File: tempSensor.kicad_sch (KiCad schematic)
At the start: 5 parts, among them U2 TMP175AIDR

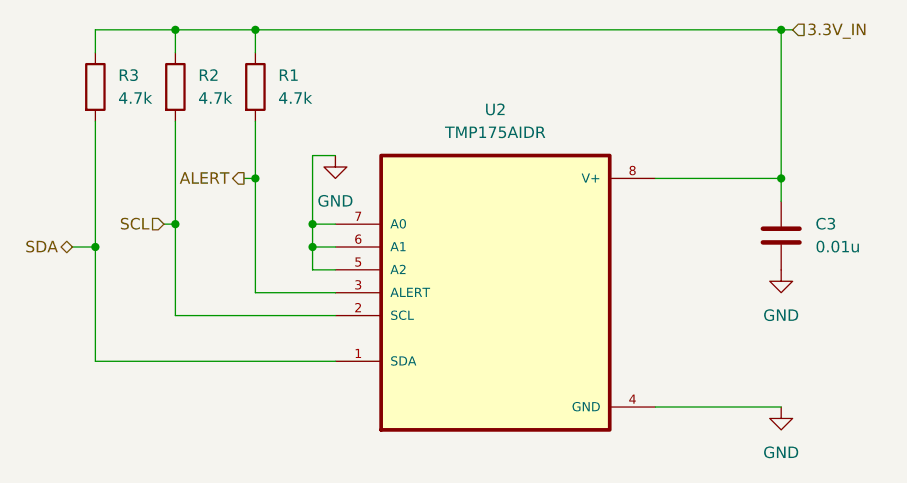
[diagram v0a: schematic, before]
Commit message: Finished PCB
Also added GNDA and GNDD references, to be changed back to GND later. Also added wires connecting ground polygons
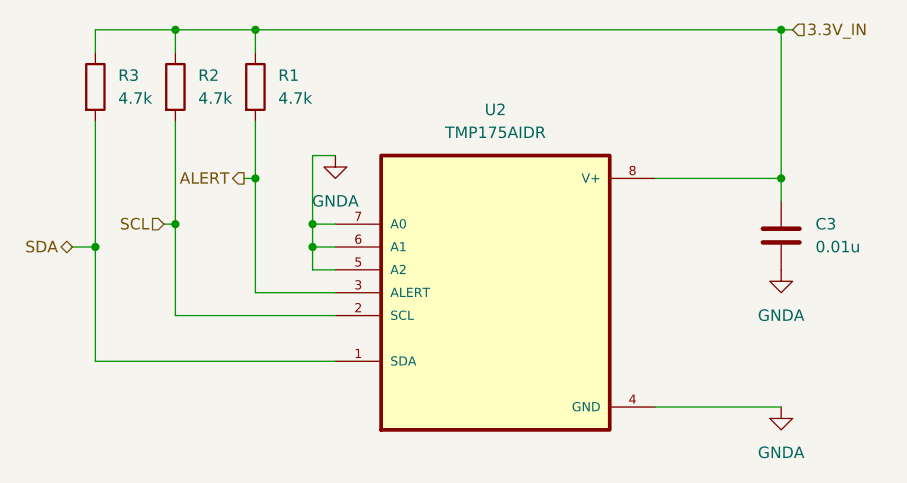
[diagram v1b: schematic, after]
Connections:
- net GND renamed GNDA
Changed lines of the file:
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@@
 	)
 	(symbol
-		(lib_id "power:GND")
+		(lib_id "power:GNDA")
 		(at 170.18 96.52 0)
 		(unit 1)
@@
 			)
 		)
-		(property "Value" "GND"
+		(property "Value" "GNDA"
 			(at 170.18 101.6 0)
 			(effects
@@
 			)
 		)
-		(property "Description" "Power symbol creates a global label with name \"GND\" , ground"
+		(property "Description" "Power symbol creates a global label with name \"GNDA\" , analog ground"
 			(at 170.18 96.52 0)
 			(effects
@@
 	)
 	(symbol
-		(lib_id "power:GND")
+		(lib_id "power:GNDA")
 		(at 120.65 68.58 0)
 		(unit 1)
@@
 			)
 		)
-		(property "Value" "GND"
+		(property "Value" "GNDA"
 			(at 120.65 73.66 0)
 			(effects
@@
 			)
 		)
-		(property "Description" "Power symbol creates a global label with name \"GND\" , ground"
+		(property "Description" "Power symbol creates a global label with name \"GNDA\" , analog ground"
 			(at 120.65 68.58 0)
 			(effects
@@
 	)
 	(symbol
-		(lib_id "power:GND")
+		(lib_id "power:GNDA")
 		(at 170.18 81.28 0)
 		(unit 1)
@@
 			)
 		)
-		(property "Value" "GND"
+		(property "Value" "GNDA"
 			(at 170.18 86.36 0)
 			(effects
@@
 			)
 		)
-		(property "Description" "Power symbol creates a global label with name \"GND\" , ground"
+		(property "Description" "Power symbol creates a global label with name \"GNDA\" , analog ground"
 			(at 170.18 81.28 0)
 			(effects

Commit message: Changed grounds and began with new planes
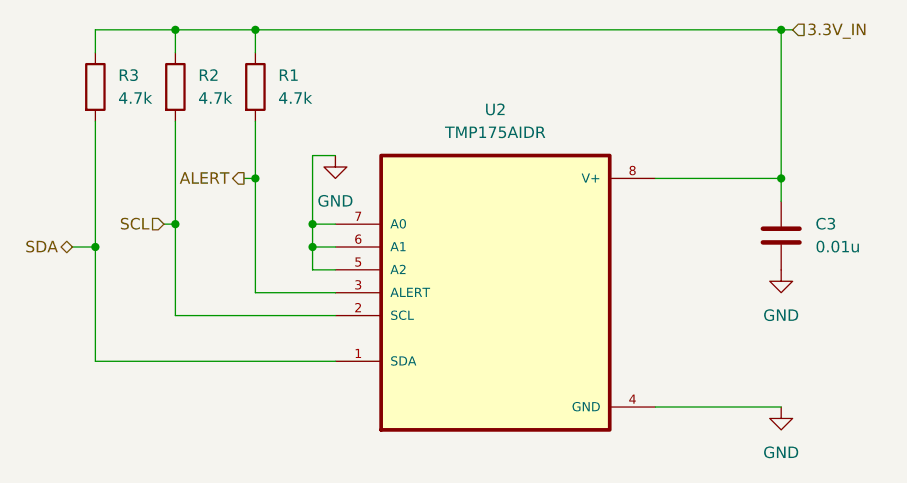
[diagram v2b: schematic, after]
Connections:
- net GNDA renamed GND
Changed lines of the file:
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@@
 	)
 	(symbol
-		(lib_id "power:GNDA")
+		(lib_id "power:GND")
 		(at 170.18 96.52 0)
 		(unit 1)
@@
 		(dnp no)
 		(fields_autoplaced yes)
-		(property "Reference" "#PWR029"
+		(property "Reference" "#PWR29"
 			(at 170.18 102.87 0)
 			(effects
@@
 			)
 		)
-		(property "Value" "GNDA"
+		(property "Value" "GND"
 			(at 170.18 101.6 0)
 			(effects
@@
 			)
 		)
-		(property "Description" "Power symbol creates a global label with name \"GNDA\" , analog ground"
+		(property "Description" "Power symbol creates a global label with name \"GND\" , ground"
 			(at 170.18 96.52 0)
 			(effects
@@
 			(project "plant caretaker"
 				(path "/23b35dcc-615e-4aec-abee-c26cc3d8b906/f322dacc-209e-46f8-9f8f-6103b236b6bb"
-					(reference "#PWR029")
+					(reference "#PWR29")
 					(unit 1)
 				)
@@
 	)
 	(symbol
-		(lib_id "power:GNDA")
+		(lib_id "power:GND")
 		(at 120.65 68.58 0)
 		(unit 1)
@@
 		(dnp no)
 		(fields_autoplaced yes)
-		(property "Reference" "#PWR031"
+		(property "Reference" "#PWR31"
 			(at 120.65 74.93 0)
 			(effects
@@
 			)
 		)
-		(property "Value" "GNDA"
+		(property "Value" "GND"
 			(at 120.65 73.66 0)
 			(effects
@@
 			)
 		)
-		(property "Description" "Power symbol creates a global label with name \"GNDA\" , analog ground"
+		(property "Description" "Power symbol creates a global label with name \"GND\" , ground"
 			(at 120.65 68.58 0)
 			(effects
@@
 			(project "plant caretaker"
 				(path "/23b35dcc-615e-4aec-abee-c26cc3d8b906/f322dacc-209e-46f8-9f8f-6103b236b6bb"
-					(reference "#PWR031")
+					(reference "#PWR31")
 					(unit 1)
 				)
@@
 	)
 	(symbol
-		(lib_id "power:GNDA")
+		(lib_id "power:GND")
 		(at 170.18 81.28 0)
 		(unit 1)
@@
 		(dnp no)
 		(fields_autoplaced yes)
-		(property "Reference" "#PWR032"
+		(property "Reference" "#PWR32"
 			(at 170.18 87.63 0)
 			(effects
@@
 			)
 		)
-		(property "Value" "GNDA"
+		(property "Value" "GND"
 			(at 170.18 86.36 0)
 			(effects
@@
 			)
 		)
-		(property "Description" "Power symbol creates a global label with name \"GNDA\" , analog ground"
+		(property "Description" "Power symbol creates a global label with name \"GND\" , ground"
 			(at 170.18 81.28 0)
 			(effects
@@
 			(project "plant caretaker"
 				(path "/23b35dcc-615e-4aec-abee-c26cc3d8b906/f322dacc-209e-46f8-9f8f-6103b236b6bb"
-					(reference "#PWR032")
+					(reference "#PWR32")
 					(unit 1)
 				)
